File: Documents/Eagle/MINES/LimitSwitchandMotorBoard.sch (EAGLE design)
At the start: 10 parts, among them IC1 ULN2003AN, IC2 ULN2003AN, X10 B5B-XH-2, X11 B2B-XH-2, X12 B2B-XH-2, X13 B2B-XH-2, X14 B2B-XH-2, X15 B2B-XH-2, X9 B5B-XH-2

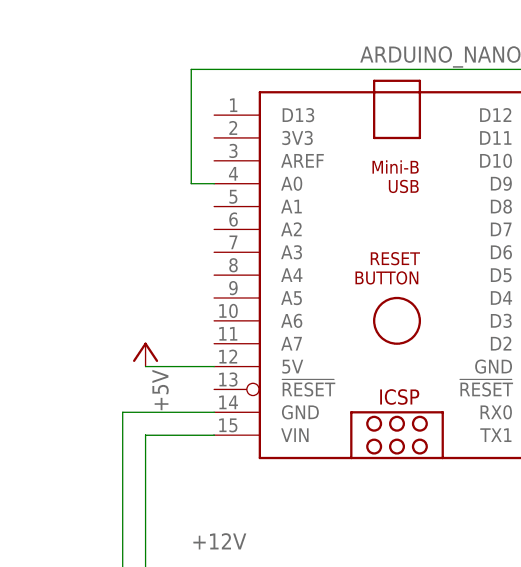
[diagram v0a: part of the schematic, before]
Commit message: Added 3-head breakouts to both boards and team name
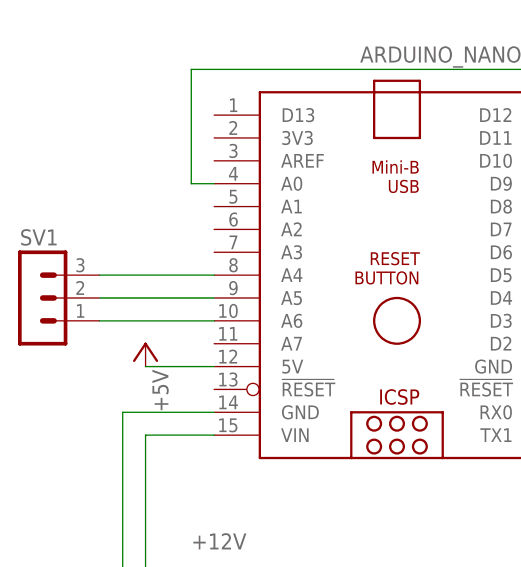
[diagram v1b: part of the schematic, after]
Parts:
- added SV1: (no value), con-lstb:MA03-1
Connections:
- new net N$20: ARDUINO_NANO2.A4, SV1.3
- new net N$21: ARDUINO_NANO2.A5, SV1.2
- new net N$22: ARDUINO_NANO2.A6, SV1.1
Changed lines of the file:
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@@
 <part name="GND17" library="supply1" library_urn="urn:adsk.eagle:library:371" deviceset="GND" device=""/>
 <part name="P+8" library="supply1" library_urn="urn:adsk.eagle:library:371" deviceset="+5V" device=""/>
+<part name="SV1" library="con-lstb" library_urn="urn:adsk.eagle:library:162" deviceset="MA03-1" device="" package3d_urn="urn:adsk.eagle:package:8339/1"/>
 </parts>
 <sheets>
@@
 <instance part="P+8" gate="1" x="-27.94" y="20.32" smashed="yes">
 <attribute name="VALUE" x="-25.4" y="12.7" size="1.778" layer="96" rot="R90"/>
+</instance>
+<instance part="SV1" gate="G$1" x="-40.64" y="25.4" smashed="yes">
+<attribute name="VALUE" x="-41.91" y="17.78" size="1.778" layer="96"/>
+<attribute name="NAME" x="-41.91" y="31.242" size="1.778" layer="95"/>
 </instance>
 </instances>
@@
 </segment>
 </net>
+<net name="N$20" class="0">
+<segment>
+<pinref part="ARDUINO_NANO2" gate="G$1" pin="A4"/>
+<pinref part="SV1" gate="G$1" pin="3"/>
+<wire x1="-20.32" y1="27.94" x2="-33.02" y2="27.94" width="0.1524" layer="91"/>
+</segment>
+</net>
+<net name="N$21" class="0">
+<segment>
+<pinref part="SV1" gate="G$1" pin="2"/>
+<pinref part="ARDUINO_NANO2" gate="G$1" pin="A5"/>
+<wire x1="-33.02" y1="25.4" x2="-20.32" y2="25.4" width="0.1524" layer="91"/>
+</segment>
+</net>
+<net name="N$22" class="0">
+<segment>
+<pinref part="ARDUINO_NANO2" gate="G$1" pin="A6"/>
+<pinref part="SV1" gate="G$1" pin="1"/>
+<wire x1="-20.32" y1="22.86" x2="-33.02" y2="22.86" width="0.1524" layer="91"/>
+</segment>
+</net>
